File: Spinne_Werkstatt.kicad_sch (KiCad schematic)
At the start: 17 parts, among them J1 Conn_01x02_Pin, J3 Conn_01x03_Pin, Q1 BSS138, Q2 BSS138, U1 ESP32-WROOM-32UE, U2 CH340C

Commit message: added gerber
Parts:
- renumbered Spannungsregler1 to AMS1117, ESP_EN_R to ESP_EN_R1
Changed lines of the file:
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@@
 		(dnp no)
 		(fields_autoplaced yes)
-		(property "Reference" "Spannungsregler1"
+		(property "Reference" "AMS1117"
 			(at 224.79 49.53 0)
 			(effects
@@
 			(project "Spinne_Werkstatt"
 				(path "/63f5a8da-c9e8-4b26-9a17-2dbcdac59688"
-					(reference "Spannungsregler1")
+					(reference "AMS1117")
 					(unit 1)
 				)
@@
 		(dnp no)
 		(fields_autoplaced yes)
-		(property "Reference" "ESP_EN_R"
+		(property "Reference" "ESP_EN_R1"
 			(at 379.73 46.9899 0)
 			(effects
@@
 			(project ""
 				(path "/63f5a8da-c9e8-4b26-9a17-2dbcdac59688"
-					(reference "ESP_EN_R")
-					(unit 1)
-				)
+					(reference "ESP_EN_R1")
+					(unit 1)
+				)

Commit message: changed elko footprints, changed voltage regulator footprint
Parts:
- AMS1117: footprint Package_TO_SOT_SMD:SOT-223-3_TabPin2 -> bulme_footprints:SOT230P700X180-4N
- C_3.3V1, C_5V1, C_ESP1: footprint Capacitor_SMD:CP_Elec_5x5.7 -> Capacitor_SMD:CP_Elec_5x5.4
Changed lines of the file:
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@@
 			)
 		)
-		(property "Footprint" "Package_TO_SOT_SMD:SOT-223-3_TabPin2"
+		(property "Footprint" "bulme_footprints:SOT230P700X180-4N"
 			(at 224.79 50.8 0)
 			(effects
@@
 			)
 		)
-		(property "Footprint" "Capacitor_SMD:CP_Elec_5x5.7"
+		(property "Footprint" "Capacitor_SMD:CP_Elec_5x5.4"
 			(at 36.83 157.48 0)
 			(effects
@@
 			)
 		)
-		(property "Footprint" "Capacitor_SMD:CP_Elec_5x5.7"
+		(property "Footprint" "Capacitor_SMD:CP_Elec_5x5.4"
 			(at 208.28 60.96 0)
 			(effects
@@
 			)
 		)
-		(property "Footprint" "Capacitor_SMD:CP_Elec_5x5.7"
+		(property "Footprint" "Capacitor_SMD:CP_Elec_5x5.4"
 			(at 240.03 60.96 0)
 			(effects

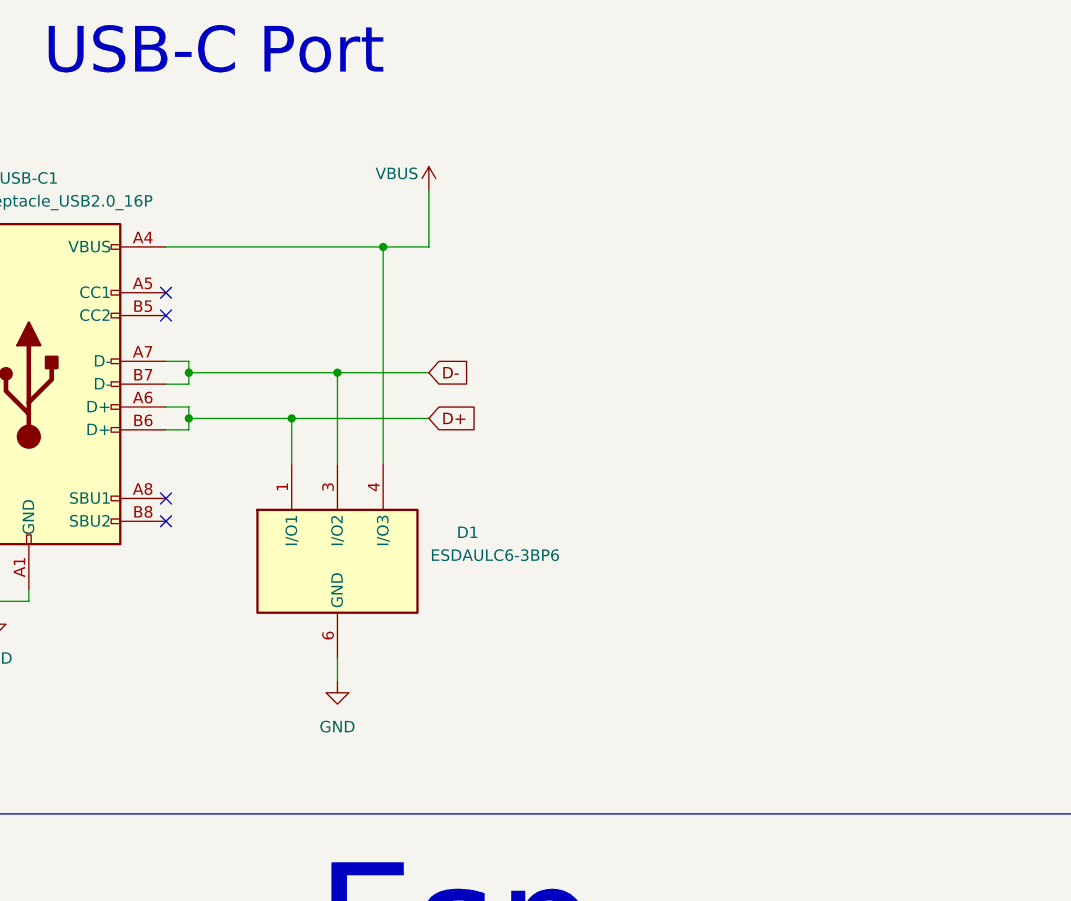
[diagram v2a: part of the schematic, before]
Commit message: added additional USB data protection, not pretty -- version 1.1.3
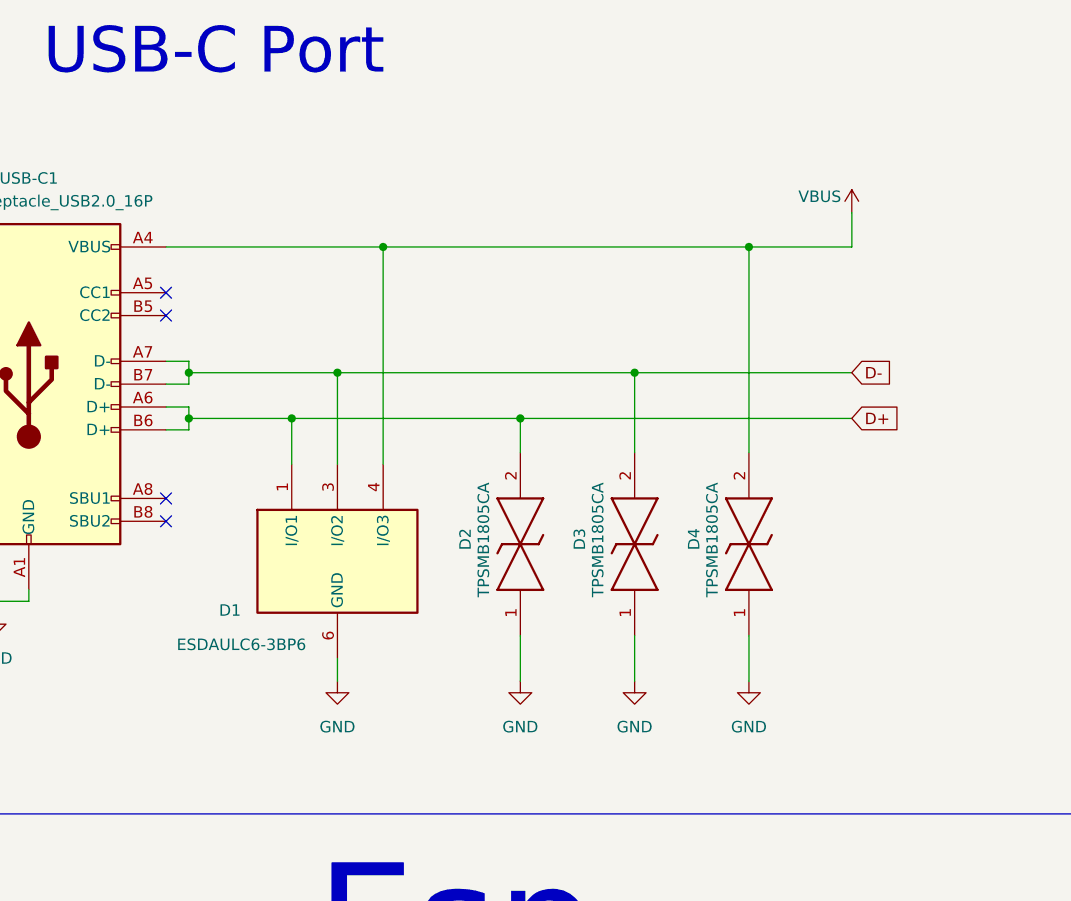
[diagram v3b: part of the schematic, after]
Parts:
- added D2, D3, D4: TPSMB1805CA, bulme_footprints:TPSMB1805CA, symbol bulme_schematics:TPSMB1805CA
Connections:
- net D+: now also D2.2
- net D-: now also D3.2
- net GND: now also D2.1, D3.1, D4.1
- net VBUS: now also D4.2
